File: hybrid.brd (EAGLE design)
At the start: 99.1 x 82.5 mm, 59 parts, among them J1 RCJ-21XXMILL, J3 NRJ3HF-1, Q1 BC560KINKED, Q10 BC550KINKED, Q11 BC550KINKED, Q12 BC560KINKED, Q13 BD140, Q14 BD139, Q2 BC556KINKED, Q3 BC550KINKED, Q4 BC550KINKED, Q5 BC560KINKED, Q6 BD140, Q7 BD139, Q8 BC560KINKED, Q9 BC556KINKED

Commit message: Mounting holes, caps layout
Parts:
- added H1, H2: MOUNT-PAD-ROUND3.2, holes:3,2-PAD
- C1, C4, C5, C7: value (none) -> 47uF; device my-cap:CPOL-RADIAL-6.5/2.5 -> my-cap:CPOL-RADIAL-8/3.5
- C2, C6: device my-cap:CPOL-RADIAL-1000UF-25V -> my-cap:CPOL-RADIAL-8/3.5
- C3, C8: device my-cap:CPOL-RADIAL-1000UF-63V -> my-cap:CPOL-RADIAL-16/7.5
- moved J4 2.54 mm to (2.54, 72.4)
- moved C4 1.27 mm to (8.89, 27.9), turned to 0 degrees
- moved C7 1.27 mm to (90.2, 27.9)
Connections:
- net FB_L: now also C2.1; no longer C2.+
- net FB_R: now also C6.1; no longer C6.+
- net GND: now also H1.B3,2, H2.B3,2
- net N$19: now also C6.2; no longer C6.-
- net N$4: now also C2.2; no longer C2.-
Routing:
- net HT: track 152.0 -> 151.1 mm
- net VCC: track 208.7 -> 207.7 mm
- net FB_R: track 47.8 -> 48.6 mm
- net N$4: track 6.02 -> 6.81 mm
- net FB_L: track 47.8 -> 48.6 mm
- net N$19: track 6.02 -> 6.81 mm

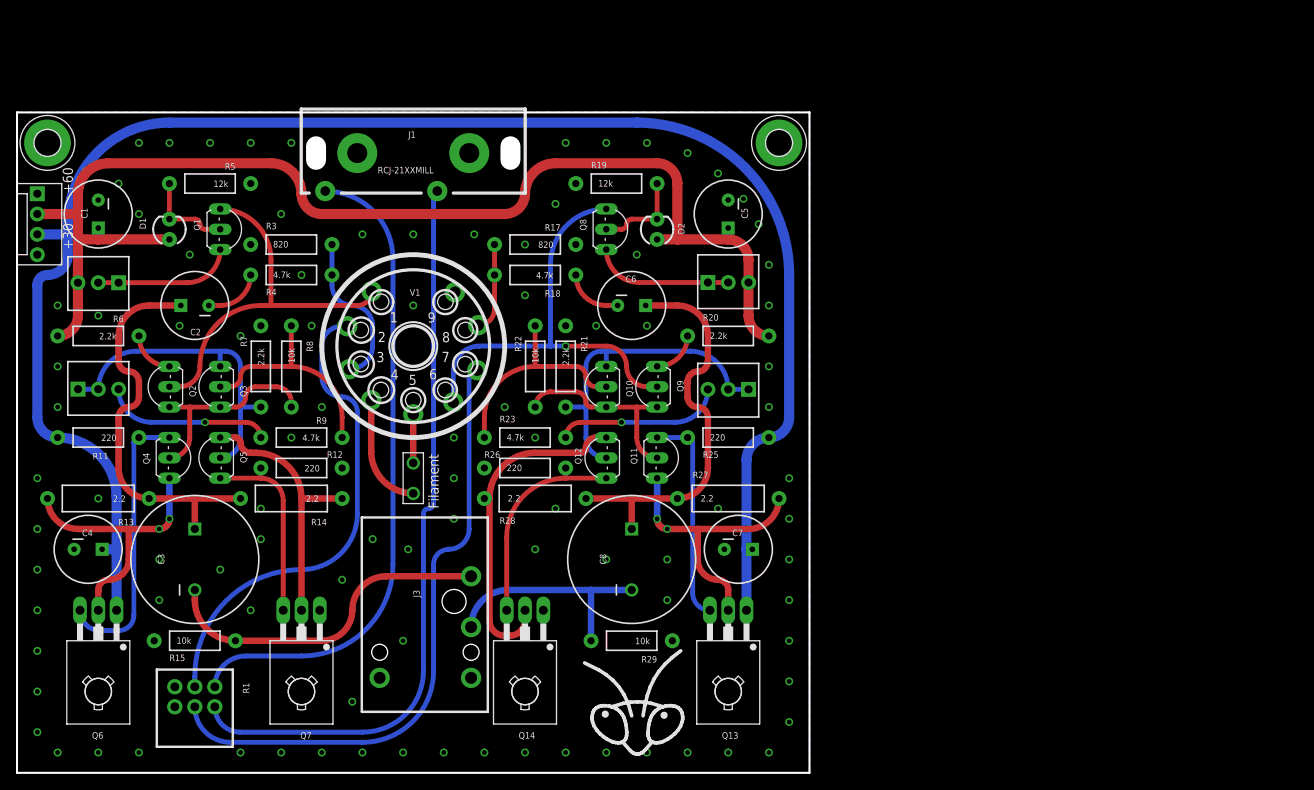
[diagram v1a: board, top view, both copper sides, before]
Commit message: Amp + PS on the same board. Rerouted from scratch
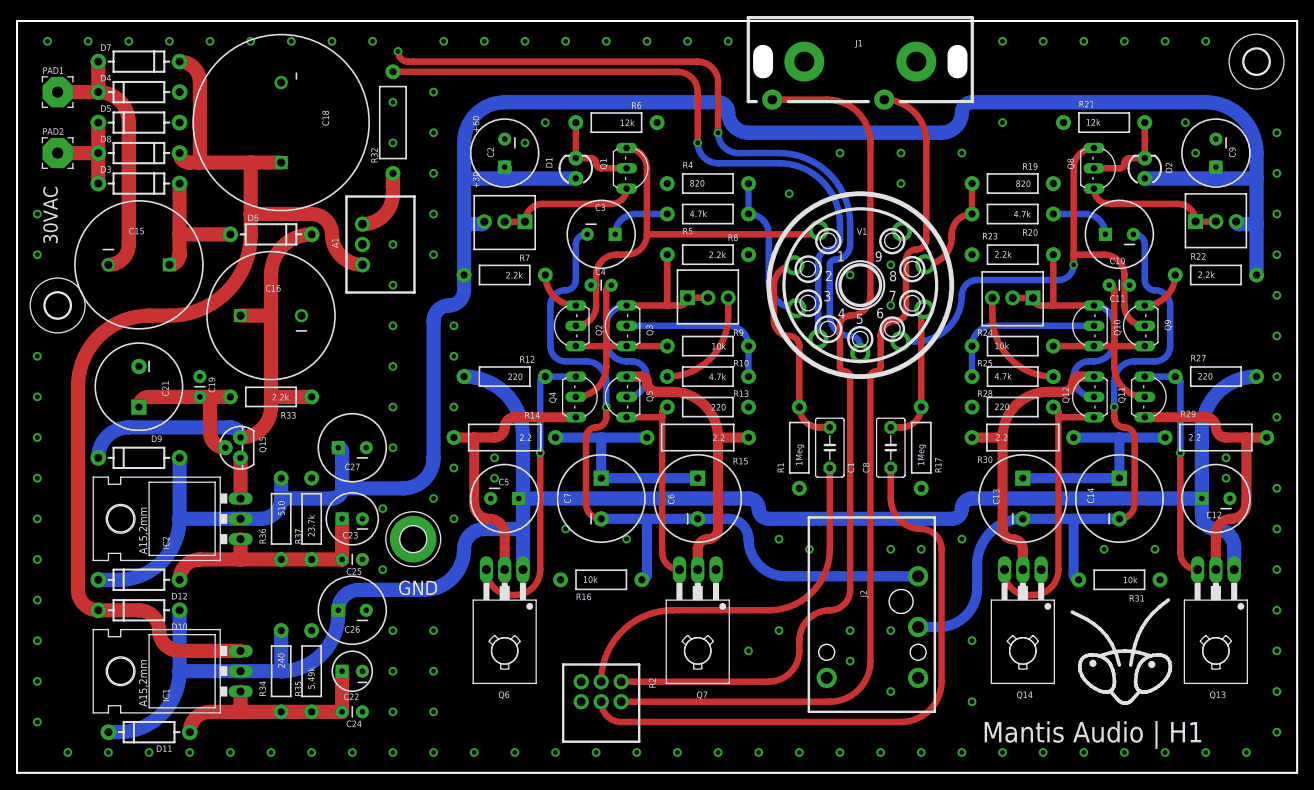
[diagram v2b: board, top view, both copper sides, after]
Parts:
- removed J3: NRJ3HF-1, my-conn:NRJ3HF
- removed J4: (no value), SparkFun-Connectors:MOLEX-1X4
- added A1: R-78HBXX-0.5, my-smps:R-78HB
- added C10, C12, C26, C27, C9: 47uF, my-cap:CPOL-RADIAL-8/3.5
- added C11: 10p, SparkFun-Capacitors:CAP-PTH-SMALL
- added C13, C14: 470uF, my-cap:CPOL-RADIAL-12/5
- added C15, C16: 470uF, my-cap:CPOL-RADIAL-16/7.5
- added C18: 4700uF, my-cap:CPOL-RADIAL-22/10
- added C19, C24, C25: 1uF, SparkFun-Capacitors:CAP-PTH-SMALL
- added C21: 47uF, my-cap:CPOL-RADIAL-12/5
- added C22: 10uF, my-cap:CPOL-RADIAL-5/2.5
- added C23: 10uF, my-cap:CPOL-RADIAL-6.5/2.5
- added D10, D11, D12, D3, D4, D5, D6, D7, D8, D9: (no value), SparkFun-DiscreteSemi:DIODE-1N4001
- added GB1: (no value), my:COPPER-BRIDGE-SM
- added H3: MOUNT-HOLE3.2, holes:3,2
- added IC1, IC2: LM317MABT, v-reg:TO220L1
- added PAD1: 30VAC_H, wirepad:3,81/1,4
- added PAD2: 30VAC_L, wirepad:3,81/1,4
- added Q15: KSP43, my-tran:TO-92
- added R30: 2.2, SparkFun-Resistors:AXIAL-0.5
- added R31: 10k, SparkFun-Resistors:AXIAL-0.4
- added R32: 0.536, my-res:AXIAL-0.5
- added R33: 2.2k, SparkFun-Resistors:AXIAL-0.4
- added R34: 240, SparkFun-Resistors:AXIAL-0.4
- added R35: 5.49k, SparkFun-Resistors:AXIAL-0.4
- added R36: 510, SparkFun-Resistors:AXIAL-0.4
- added R37: 23.7k, SparkFun-Resistors:AXIAL-0.4
- C1: value 47uF -> 0.47u; device my-cap:CPOL-RADIAL-8/3.5 -> capacitor-wima:C5B3.5
- C3: value 470uF -> 47uF; device my-cap:CPOL-RADIAL-16/7.5 -> my-cap:CPOL-RADIAL-8/3.5
- C4: value 47uF -> 10p; device my-cap:CPOL-RADIAL-8/3.5 -> SparkFun-Capacitors:CAP-PTH-SMALL
- C6, C7: value 47uF -> 470uF; device my-cap:CPOL-RADIAL-8/3.5 -> my-cap:CPOL-RADIAL-12/5
- C8: value 470uF -> 0.47u; device my-cap:CPOL-RADIAL-16/7.5 -> capacitor-wima:C5B3.5
- H2: value MOUNT-PAD-ROUND3.2 -> MOUNT-HOLE3.2; device holes:3,2-PAD -> holes:3,2
- J2: value (none) -> NRJ3HF-1; device SparkFun-Connectors:1X02_BIG -> my-conn:NRJ3HF
- R1: value TD90 -> 1Meg; device my:PTD902 -> SparkFun-Resistors:AXIAL-0.4
- R10: value 10k -> 4.7k; device SparkFun-Electromechanical:3362U-2 -> SparkFun-Resistors:AXIAL-0.4
- R11, R26: value 220 -> 10k; device SparkFun-Resistors:AXIAL-0.4 -> SparkFun-Electromechanical:3362U-2
- R13, R27, R28: value 2.2 -> 220; device SparkFun-Resistors:AXIAL-0.5 -> SparkFun-Resistors:AXIAL-0.4
- R15, R29: value 10k -> 2.2; device SparkFun-Resistors:AXIAL-0.4 -> SparkFun-Resistors:AXIAL-0.5
- R16: value 1k -> 10k; device SparkFun-Electromechanical:3362U-2 -> SparkFun-Resistors:AXIAL-0.4
- R17: value 820 -> 1Meg
- R18: value 4.7k -> 1k; device SparkFun-Resistors:AXIAL-0.4 -> SparkFun-Electromechanical:3362U-2
- R19: value 12k -> 820
- R2: value 1k -> TD90; device SparkFun-Electromechanical:3362U-2 -> my:PTD902
- R20: value 2.2k -> 4.7k
- R21, R6: value 2.2k -> 12k
- R22, R8: value 10k -> 2.2k
- R23: value 4.7k -> 2.2k
- R24: device SparkFun-Electromechanical:3362U-2 -> SparkFun-Resistors:AXIAL-0.4
- R25: value 220 -> 4.7k
- R3: value 820 -> 1k; device SparkFun-Resistors:AXIAL-0.4 -> SparkFun-Electromechanical:3362U-2
- R4: value 4.7k -> 820
- R5: value 12k -> 4.7k
- R9: value 4.7k -> 10k
- moved C1 96.0 mm to (101.6, 40.6), turned to 90 degrees
- moved R22 85.9 mm to (149.9, 62.2), turned to 0 degrees
- moved R18 85.4 mm to (149.9, 69.2), turned to 0 degrees
- moved R1 82.2 mm to (97.8, 40.6), turned to 90 degrees
- moved R2 81.6 mm to (73.0, 8.89), turned to 270 degrees
- moved R11 78.2 mm to (86.4, 59.7), turned to 0 degrees
- moved R29 77.3 mm to (149.9, 41.9), turned to 0 degrees
- moved R13 77.1 mm to (86.4, 45.7)
- moved R10 76.2 mm to (86.4, 49.5), turned to 180 degrees
- moved R21 73.9 mm to (135.9, 81.3), turned to 0 degrees
- moved C4 71.0 mm to (71.8, 61.0)
- moved R6 70.0 mm to (74.9, 81.3)
- moved R15 67.8 mm to (85.1, 41.9), turned to 180 degrees
- moved H1 67.4 mm to (49.5, 29.2)
- moved R23 65.1 mm to (124.5, 64.8)
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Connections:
- removed net N$1: J2.P$2, V1.4
- removed net N$6: J2.P$1, V1.5
- new net +6.3FIL: R32.P$2, V1.4
- new net +LV: A1.1, C18.1, D10.C, D7.C, D8.C, IC1.3
- new net 30VAC_H: C15.2, D4.C, D7.A, PAD1.1
- new net 30VAC_L: D3.A, D5.C, D8.A, PAD2.1
- new net N$18: C8.2, R17.P$2, V1.7
- new net N$30: C22.1, C24.1, D11.A, IC1.1, R34.P$2, R35.P$1
- new net N$31: C15.1, D3.C, D6.A
- new net N$32: A1.3, R32.P$1
- new net N$33: C16.1, D6.C, D9.C, Q15.3, R33.P$1
- new net N$34: C19.1, C21.+, Q15.2, R33.P$2
- new net N$36: C23.1, C25.1, D12.A, IC2.1, R36.P$2, R37.P$1
- new net N$37: IC2.3, Q15.1
- new net N$9: C1.2, R1.P$2, V1.2
- new net SGND: GB1.2, V1.5
- net CAT_L: now also R5.P$2; no longer R3.P$2
- net CAT_R: now also R19.P$2, R20.P$2; no longer R17.P$2, R18.P$2
- net FB_L: now also C6.+, C7.+, R14.P$1, R15.P$2; no longer C2.1, C3.1, R13.P$1, R14.P$2
- net FB_R: now also C13.+, C14.+, R29.P$1, R30.P$2; no longer C6.1, C8.1, R27.P$1, R28.P$2
- net GND: now also A1.2, C12.2, C16.2, C18.2, C19.2, C2.2, C21.-, C22.2, C23.2, C24.2, C25.2, C26.2, C27.2, C9.2, D4.A, D5.A, GB1.1, J2.S, R1.P$1, R13.P$1, R16.P$1, R2.R1.1, R2.R2.1, R23.P$1, R28.P$1, R31.P$1, R35.P$2, R37.P$2, R4.P$1, R6.P$1, R8.P$1; no longer C1.2, C4.2, C7.2, H2.B3,2, J3.S, J4.1, J4.4, R1.R1.1, R1.R2.1, R12.P$1, R15.P$1, R26.P$1, R29.P$1, R3.P$1, R5.P$1, R7.P$1
- net HT: now also C2.1, C27.1, C9.1, D12.C, D9.A, IC2.2, R18.3, R22.P$2, R3.3, R36.P$1, R7.P$2; no longer C1.1, C5.1, J4.2, R16.3, R2.3, R20.P$2, R6.P$2
- net IN_L: now also C1.1, R2.R2.2; no longer R1.R2.2, V1.2
- net IN_L*: now also R2.R2.3; no longer R1.R2.3
- net IN_R: now also C8.1, R2.R1.2; no longer R1.R1.2, V1.7
- net IN_R*: now also R2.R1.3; no longer R1.R1.3
- net N$10: now also R10.P$2, R11.3; no longer R10.3, R9.P$2
- net N$11: now also R14.P$2; no longer R13.P$2
- net N$12: now also R11.1, R11.2, R8.P$2; no longer R10.1, R10.2, R7.P$2
- net N$13: now also R15.P$1; no longer R14.P$1
- net N$14: now also R12.P$1; no longer R11.P$1
- net N$15: now also R13.P$2; no longer R12.P$2
- net N$16: now also R18.1, R18.2; no longer R16.1, R16.2
- net N$17: now also R21.P$2; no longer R19.P$2
- net N$19: now also C10.1, R20.P$1; no longer C6.2, R18.P$1
- net N$2: now also R3.1, R3.2; no longer R2.1, R2.2
- net N$20: now also R22.P$1; no longer R20.P$1
- net N$21: now also C11.2, R24.P$2; no longer R22.P$2
- net N$22: now also R24.P$1, R25.P$1; no longer R22.P$1, R23.P$1
- net N$23: now also R25.P$2, R26.3; no longer R23.P$2, R24.3
- net N$24: now also R23.P$2, R26.1, R26.2; no longer R21.P$2, R24.1, R24.2
- net N$25: now also R29.P$2; no longer R27.P$2
- net N$26: now also R30.P$1; no longer R28.P$1
- net N$27: now also R27.P$1; no longer R25.P$1
- net N$28: now also R28.P$2; no longer R26.P$2
- net N$3: now also R6.P$2; no longer R5.P$2
- net N$4: now also C3.1, R5.P$1; no longer C2.2, R4.P$1
- net N$5: now also R7.P$1; no longer R6.P$1
- net N$7: now also C4.2, R9.P$2; no longer R8.P$2
- net N$8: now also R10.P$1; no longer R8.P$1
- net OUT_L: now also C6.-, C7.-, J2.T, R16.P$2; no longer J3.T, R15.P$2
- net OUT_R: now also C10.2, C13.-, C14.-, J2.R, R31.P$2; no longer C8.2, J3.R, R29.P$2
- net PL_L: now also C4.1
- net PL_R: now also C11.1
- net VCC: now also C12.1, C26.1, C5.1, D10.A, D11.C, IC1.2, R12.P$2, R27.P$2, R34.P$1; no longer C4.1, C7.1, J4.3, R11.P$2, R25.P$2
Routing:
- net +LV: track 0.00 -> 130.8 mm
- net HT: track 151.1 -> 262.9 mm
- net SGND: track 0.00 -> 85.5 mm, vias 0 -> 1
- net +6.3FIL: track 0.00 -> 83.0 mm, vias 0 -> 1
- net N$33: track 0.00 -> 57.9 mm
- net OUT_R: track 28.3 -> 84.2 mm, vias 0 -> 1
- net OUT_L: track 41.2 -> 94.3 mm, vias 0 -> 1
- net 30VAC_H: track 0.00 -> 33.1 mm
- net N$36: track 0.00 -> 29.0 mm
- net IN_L*: track 78.8 -> 106.6 mm
- net N$30: track 0.00 -> 27.7 mm
- net N$9: track 0.00 -> 25.0 mm
- net FB_R: track 48.6 -> 28.6 mm
- net FB_L: track 48.6 -> 28.6 mm
- net N$34: track 0.00 -> 19.1 mm
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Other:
- board size 99.1 x 82.5 mm -> 160 x 94 mm
- board text added: "30VAC"
- board text added: "GND"
- board text added: "Mantis Audio | H1"
- board text removed: "Filament"

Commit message: Small fix
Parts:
- R21, R6: value 12k -> 33k
- R32: value 0.536 -> 0.549
- V1: value (none) -> 6DJ8
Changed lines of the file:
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@@
 </element>
 <element name="R18" library="SparkFun-Electromechanical" package="3362U-2" value="1k" x="149.86" y="69.215" smashed="yes"/>
-<element name="R21" library="SparkFun-Resistors" package="AXIAL-0.4" value="12k" x="135.89" y="81.28" smashed="yes">
+<element name="R21" library="SparkFun-Resistors" package="AXIAL-0.4" value="33k" x="135.89" y="81.28" smashed="yes">
 <attribute name="NAME" x="132.715" y="83.185" size="0.8128" layer="25" font="vector" ratio="20"/>
 <attribute name="VALUE" x="133.604" y="80.899" size="0.8128" layer="21" font="vector" ratio="20"/>
@@
 <attribute name="VALUE" x="147.574" y="61.849" size="0.8128" layer="21" font="vector" ratio="20"/>
 </element>
-<element name="R6" library="SparkFun-Resistors" package="AXIAL-0.4" value="12k" x="74.93" y="81.28" smashed="yes" rot="R180">
+<element name="R6" library="SparkFun-Resistors" package="AXIAL-0.4" value="33k" x="74.93" y="81.28" smashed="yes" rot="R180">
 <attribute name="NAME" x="78.105" y="83.82" size="0.8128" layer="25" font="vector" ratio="20" rot="R180"/>
 <attribute name="VALUE" x="77.216" y="81.661" size="0.8128" layer="21" font="vector" ratio="20" rot="R180"/>
@@
 <attribute name="VALUE" x="128.905" y="18.923" size="0.8128" layer="27" ratio="20" rot="R180"/>
 </element>
-<element name="V1" library="tubes" package="NOVAL" value="" x="105.41" y="60.96" smashed="yes" rot="R180">
+<element name="V1" library="tubes" package="NOVAL" value="6DJ8" x="105.41" y="60.96" smashed="yes" rot="R180">
 <attribute name="NAME" x="106.299" y="68.072" size="0.8128" layer="25" ratio="20" rot="R180"/>
 <attribute name="VALUE" x="109.474" y="77.978" size="1.778" layer="27" ratio="10" rot="R180"/>
@@
 <attribute name="VALUE" x="52.18" y="63.04" size="0.8128" layer="27" font="fixed" ratio="20" rot="R90"/>
 </element>
-<element name="R32" library="my-res" package="AXIAL-0.5" value="0.536" x="46.99" y="81.28" smashed="yes" rot="R90">
+<element name="R32" library="my-res" package="AXIAL-0.5" value="0.549" x="46.99" y="81.28" smashed="yes" rot="R90">
 <attribute name="NAME" x="45.085" y="76.2" size="0.8128" layer="25" font="vector" ratio="20" rot="R90"/>
 <attribute name="VALUE" x="47.371" y="77.851" size="0.8128" layer="27" font="vector" ratio="20" rot="R90"/>

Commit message: Small fix
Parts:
- R16, R31: value 10k -> 2.2k
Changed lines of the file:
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@@
 <attribute name="VALUE" x="88.646" y="46.101" size="0.8128" layer="21" font="vector" ratio="20" rot="R180"/>
 </element>
-<element name="R16" library="SparkFun-Resistors" package="AXIAL-0.4" value="10k" x="73.025" y="24.13" smashed="yes">
+<element name="R16" library="SparkFun-Resistors" package="AXIAL-0.4" value="2.2k" x="73.025" y="24.13" smashed="yes">
 <attribute name="NAME" x="69.85" y="21.59" size="0.8128" layer="25" font="vector" ratio="20"/>
 <attribute name="VALUE" x="70.739" y="23.749" size="0.8128" layer="21" font="vector" ratio="20"/>
@@
 <attribute name="VALUE" x="122.174" y="45.339" size="0.8128" layer="21" font="vector" ratio="20"/>
 </element>
-<element name="R31" library="SparkFun-Resistors" package="AXIAL-0.4" value="10k" x="137.795" y="24.13" smashed="yes" rot="R180">
+<element name="R31" library="SparkFun-Resistors" package="AXIAL-0.4" value="2.2k" x="137.795" y="24.13" smashed="yes" rot="R180">
 <attribute name="NAME" x="140.97" y="22.225" size="0.8128" layer="25" font="vector" ratio="20" rot="R180"/>
 <attribute name="VALUE" x="140.081" y="24.511" size="0.8128" layer="21" font="vector" ratio="20" rot="R180"/>
